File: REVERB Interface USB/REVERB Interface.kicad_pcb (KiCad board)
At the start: 2 copper layers, 90.2 x 95.9 mm, 74 parts, among them J1 RPiZeroW, J2 Iridium, J3 APRS, J4 Antenna, J6 USB_B_Micro, J7 USB, J8 USBPOGO, M1 MountingHole_Pad, M2 MountingHole_Pad, M3 MountingHole_Pad, M4 MountingHole_Pad, M5 PiMount, M6 PiMount, M7 PiMount, M8 PiMount, U1 IMU, U2 MAX3232, U3 CY7C65213-28PVXI, U4 TXB0104D, U5 DS3232M

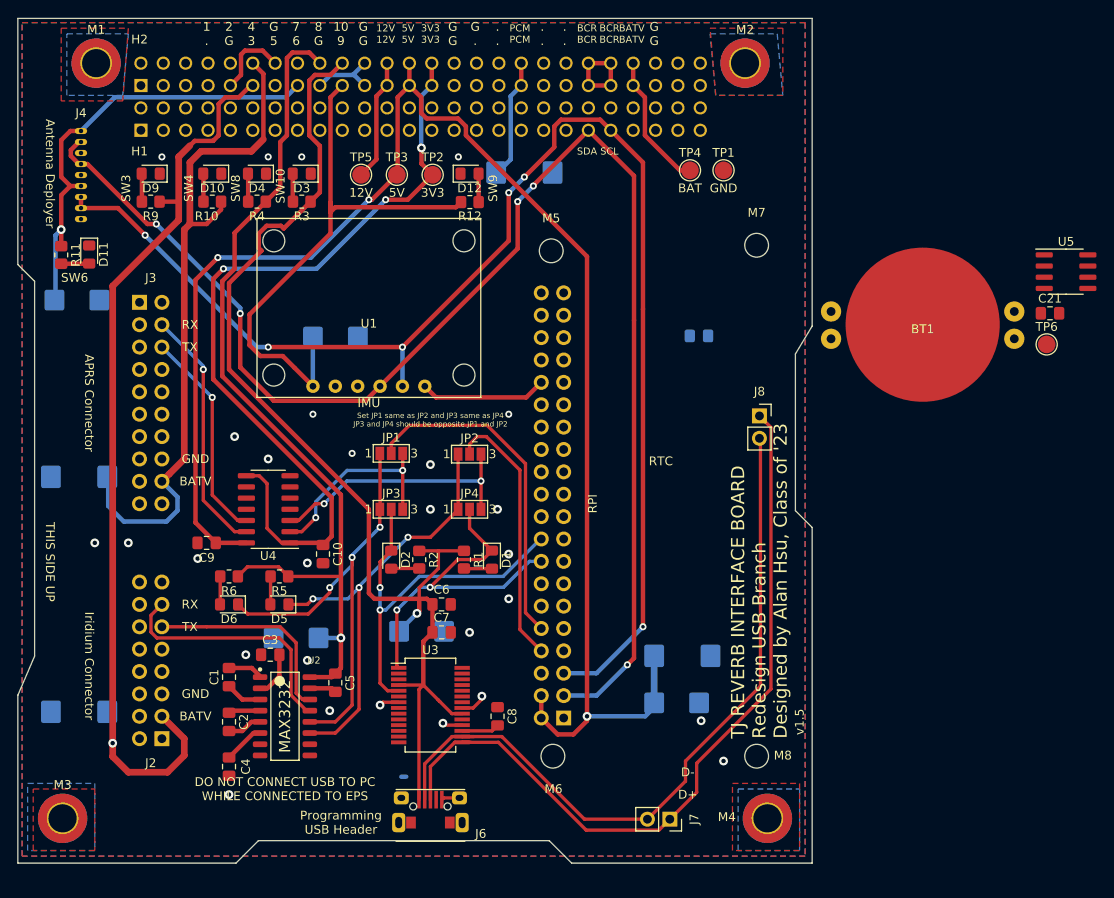
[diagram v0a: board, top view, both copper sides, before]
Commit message: add usb switch
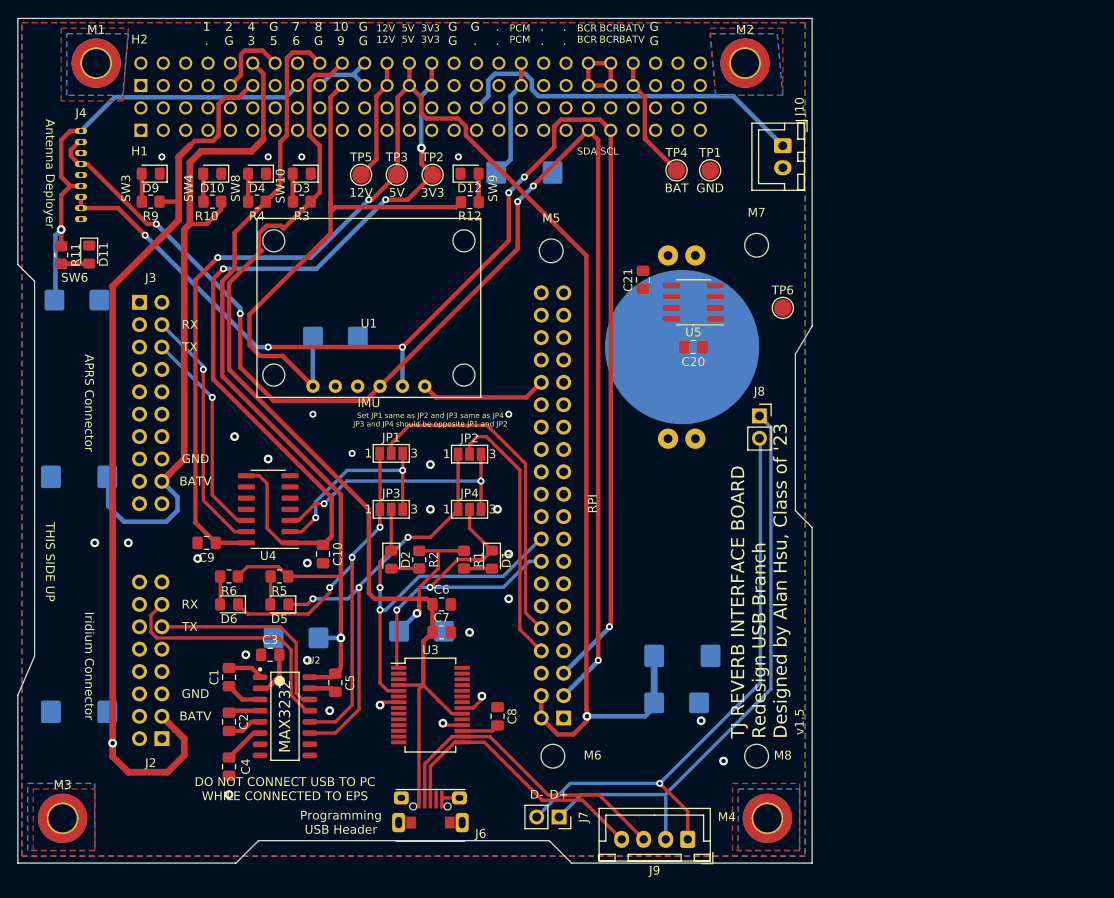
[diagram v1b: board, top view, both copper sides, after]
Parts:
- added J10: USBPWR, Connector_JST:JST_XH_B2B-XH-A_1x02_P2.50mm_Vertical, F.Cu at (193.7, 67.3)
- added J9: USB SWITCH, Connector_JST:JST_XH_B4B-XH-A_1x04_P2.50mm_Vertical, F.Cu at (182.9, 146.1)
- BT1: moved to B.Cu
- C20: moved to F.Cu
- moved C21 46.4 mm to (177.8, 82.5), turned to 90 degrees
- moved U5 42.5 mm to (183.5, 85.1), turned to 180 degrees
- moved TP6 30.2 mm to (193.7, 85.7)
- moved BT1 27.4 mm to (182.2, 90.2), turned to 90 degrees
- moved J7 12.6 mm to (168.3, 143.5)
- moved TP1 1.52 mm to (185.4, 70.1)
- moved TP4 1.52 mm to (181.6, 70.1)
- moved C20 1.42 mm to (183.5, 90.2)
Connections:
- H1 pad 32: (no net) -> /5VUSBCHG
- J7 pad 1: /D+ -> /PID+
- J7 pad 2: /D- -> /PID-
- J8 pad 1: /D+ -> /PID+
- J8 pad 2: /D- -> /PID-
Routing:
- net /PID-: track 0.00 -> 67.2 mm, vias 0 -> 1
- net /PID+: track 0.00 -> 66.6 mm
- net /D+: track 88.7 -> 32.1 mm
- net /D-: track 84.5 -> 36.4 mm
- net /5VUSBCHG: track 0.00 -> 41.4 mm
- net /EPSSDA: track 164.1 -> 158.6 mm
- net /EPSSCL: track 157.2 -> 152.0 mm
- net VBUS: track 15.5 -> 14.2 mm
- net /RI: track 0.57 -> 0.00 mm
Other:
- board text removed: "RTC"

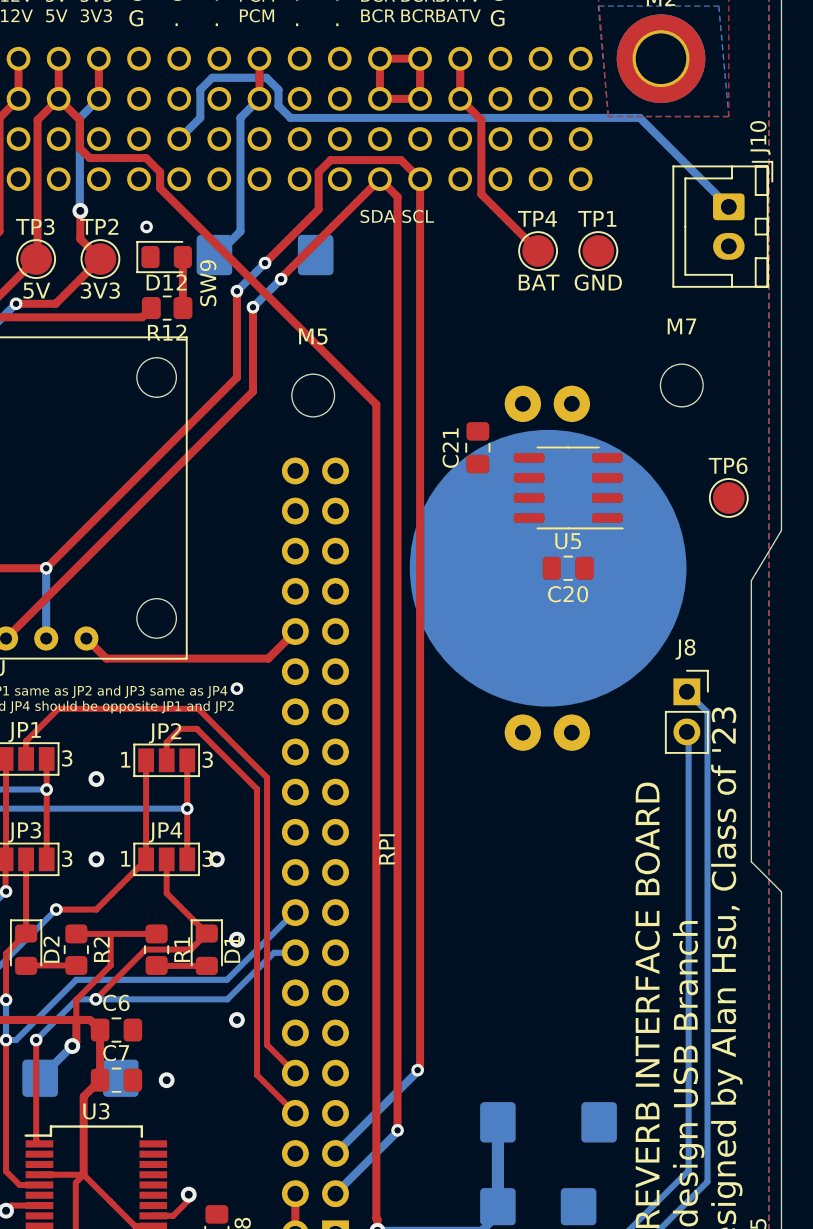
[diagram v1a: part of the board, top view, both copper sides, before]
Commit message: finish routing rtc
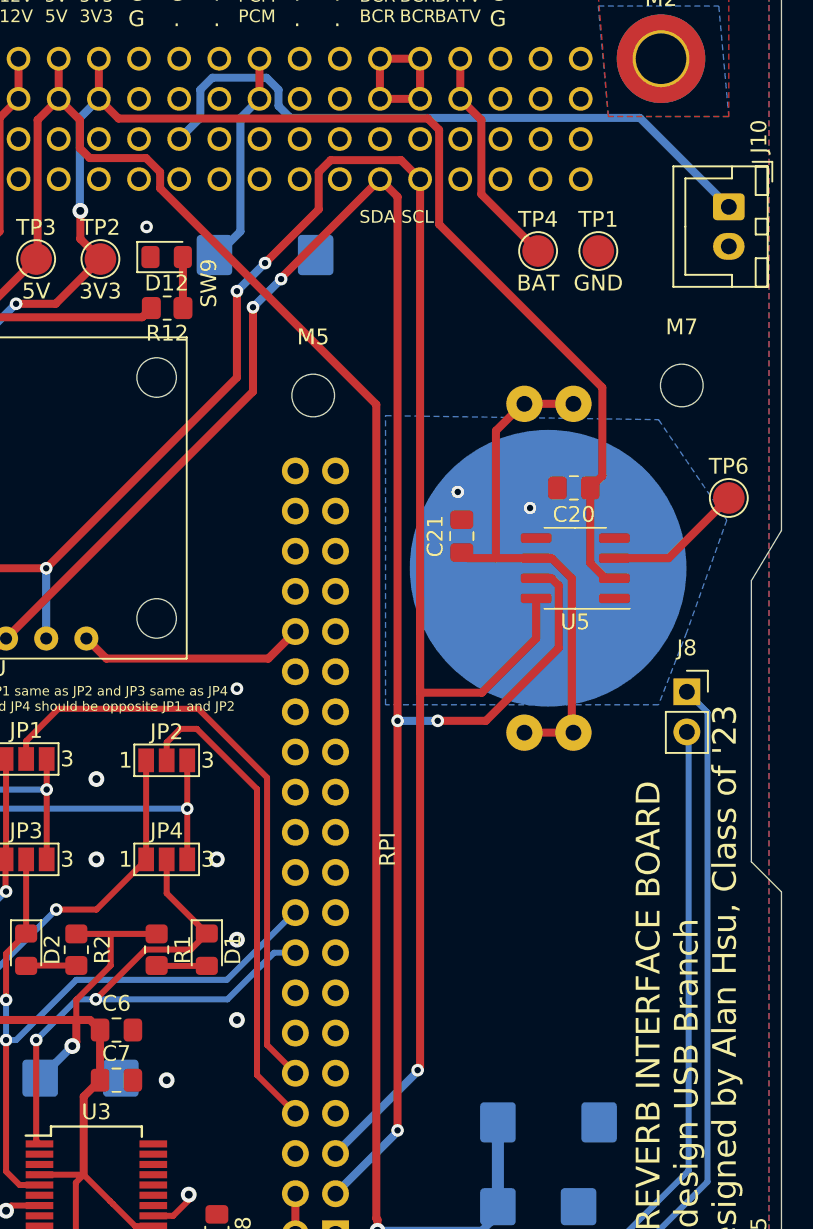
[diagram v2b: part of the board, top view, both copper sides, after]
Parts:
- moved C21 5.68 mm to (176.8, 88.1)
- moved U5 5.10 mm to (184.0, 90.2)
- moved C20 5.09 mm to (183.9, 85.1)
- turned BT1 to 270 degrees
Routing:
- net +3V3: track 94.6 -> 150.9 mm
- net Net-(BT1-Pad1): track 0.00 -> 34.2 mm
- net /EPSSDA: track 158.6 -> 176.2 mm, vias 5 -> 7
- net /EPSSCL: track 152.0 -> 169.3 mm
- net /SQW: track 0.00 -> 8.82 mm
- net GND: vias 28 -> 30

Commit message: Move some parts around, remove UART LEDs, .step export, push v1.6
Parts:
- removed D1, D5: RED, LED_SMD:LED_0805_2012Metric_Pad1.15x1.40mm_HandSolder
- removed D2, D6: GREEN, LED_SMD:LED_0805_2012Metric_Pad1.15x1.40mm_HandSolder
- removed R1, R2, R5, R6: 1K, Resistor_SMD:R_0805_2012Metric_Pad1.20x1.40mm_HandSolder
- moved R11 9.26 mm to (109.0, 70.9), turned to 180 degrees
- moved D11 8.14 mm to (109.1, 74.0), turned to 180 degrees
- moved C9 7.97 mm to (132.1, 119.4), turned to 0 degrees
- moved C13 4.86 mm to (176.8, 130.0)
- moved C11 4.83 mm to (177.5, 124.2)
- moved U4 4.20 mm to (133.5, 112.4)
- moved C10 3.92 mm to (140.2, 117.4)
- moved C16 3.85 mm to (112.0, 81.3), turned to 270 degrees
- moved JP1 3.21 mm to (146.2, 101.2)
- moved JP2 3.21 mm to (155.1, 101.3)
- moved JP3 3.21 mm to (146.2, 107.6)
- moved JP4 3.21 mm to (155.1, 107.6)
- moved J3 3.18 mm to (117.5, 85.1)
- moved J2 3.17 mm to (120.0, 134.6)
- moved BT1 2.29 mm to (180.0, 90.2)
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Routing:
- net /R1OUT: track 52.5 -> 35.9 mm, vias 3 -> 2
- net /SW8: track 101.5 -> 88.7 mm
- net /SW10: track 133.0 -> 120.4 mm
- net +5V: track 180.4 -> 188.8 mm
- net /T1IN: track 50.7 -> 42.7 mm, vias 3 -> 2
- net /APRSTXSh: track 24.2 -> 30.8 mm
- net /SW6: track 51.7 -> 45.2 mm
- net /APRSRXSh: track 28.2 -> 34.6 mm
- net /USBUARTTX: track 39.8 -> 34.0 mm
- net +3V3: track 150.9 -> 155.9 mm
- net /SW3: track 108.9 -> 105.1 mm
- net /APRSRX: track 23.1 -> 26.9 mm
- net /R1IN: track 28.3 -> 31.6 mm
- net Net-(D2-Pad2): track 3.19 -> 0.00 mm
- net Net-(D1-Pad2): track 3.19 -> 0.00 mm
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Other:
- board text added: "G"
- board text added: "PI D+"
- board text added: "PI D-"
- board text added: "UARTD+"
- board text added: "UARTD-"
- board text added: "v1.6"
- board text removed: "v1.5"

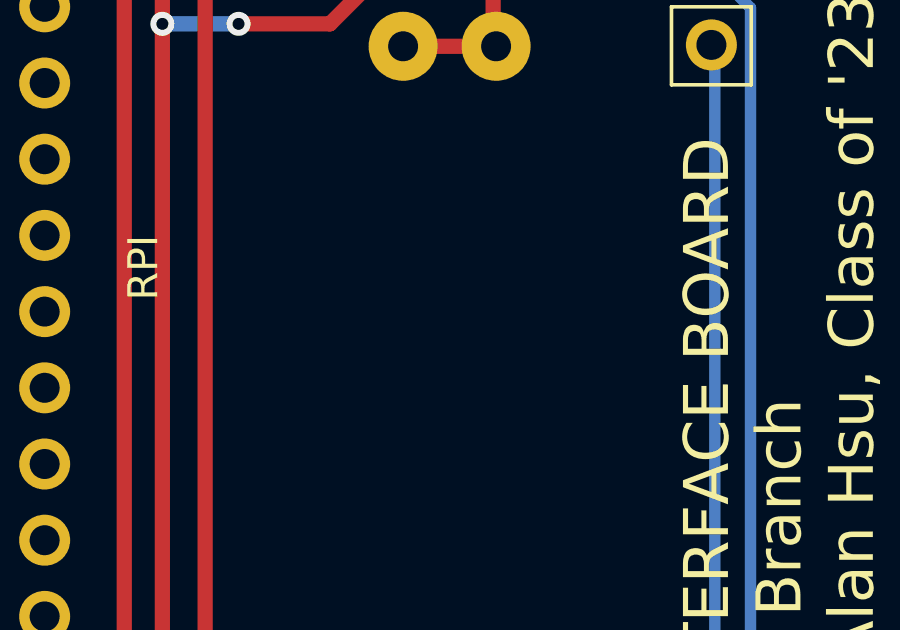
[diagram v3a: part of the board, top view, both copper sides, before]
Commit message: start on adding i2c-0 option
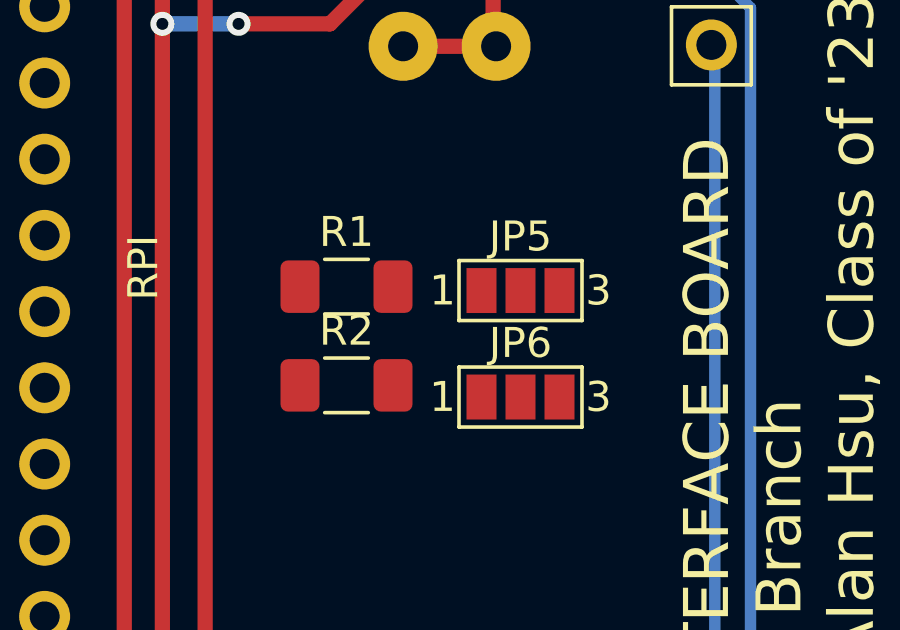
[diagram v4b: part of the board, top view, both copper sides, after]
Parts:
- added JP5: RTCSDA, Jumper:SolderJumper-3_P1.3mm_Open_Pad1.0x1.5mm_NumberLabels, F.Cu at (182.4, 108.7)
- added JP6: RTCSCL, Jumper:SolderJumper-3_P1.3mm_Open_Pad1.0x1.5mm_NumberLabels, F.Cu at (182.4, 112.3)
- added R1: 2.2K, Resistor_SMD:R_1206_3216Metric_Pad1.30x1.75mm_HandSolder, F.Cu at (176.6, 108.6)
- added R2: 2.2K, Resistor_SMD:R_1206_3216Metric_Pad1.30x1.75mm_HandSolder, F.Cu at (176.6, 111.9)
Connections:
- J1 pad 1: (no net) -> +3.3VA
- J1 pad 17: (no net) -> +3.3VA
- J1 pad 27: (no net) -> /SDA0
- J1 pad 28: (no net) -> /SCL0
- U5 pad 7: /EPSSDA -> /RTCSDA
- U5 pad 8: /EPSSCL -> /RTCSCL

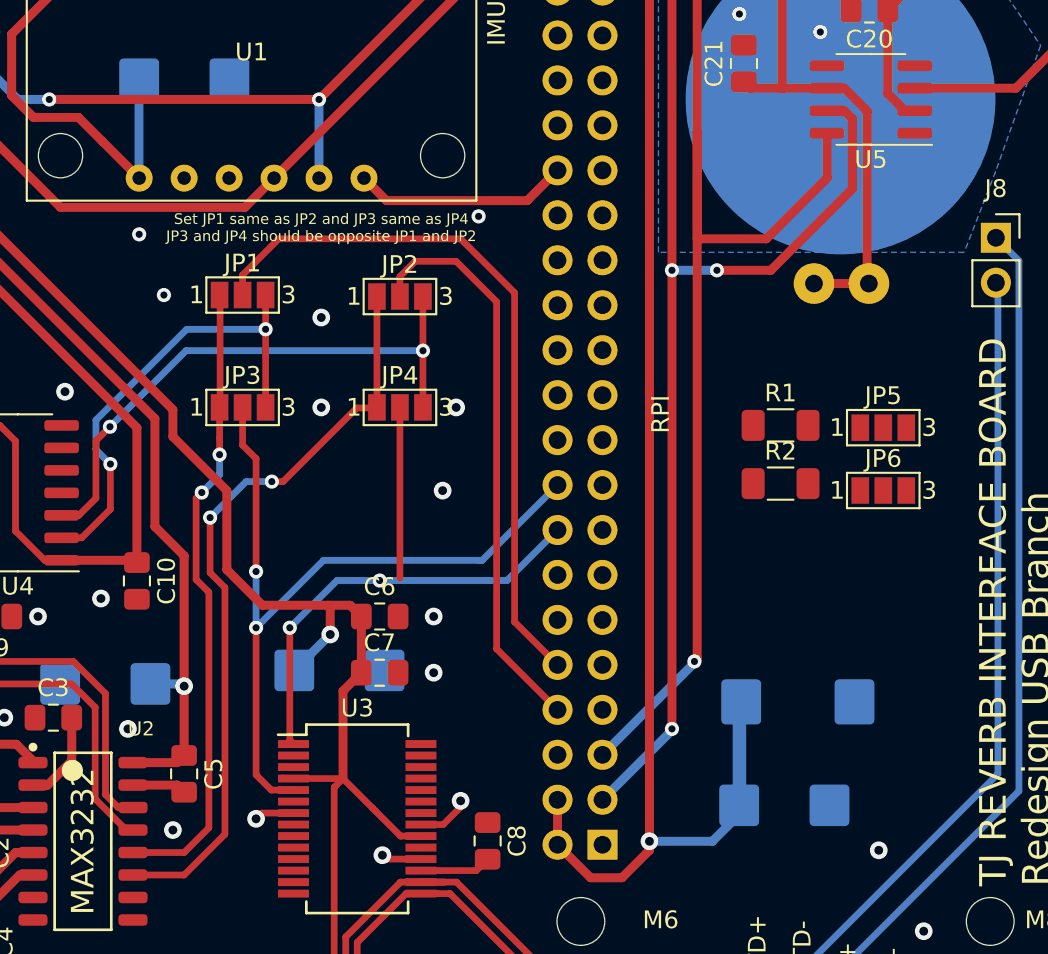
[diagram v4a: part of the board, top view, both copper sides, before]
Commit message: add i2c0 option
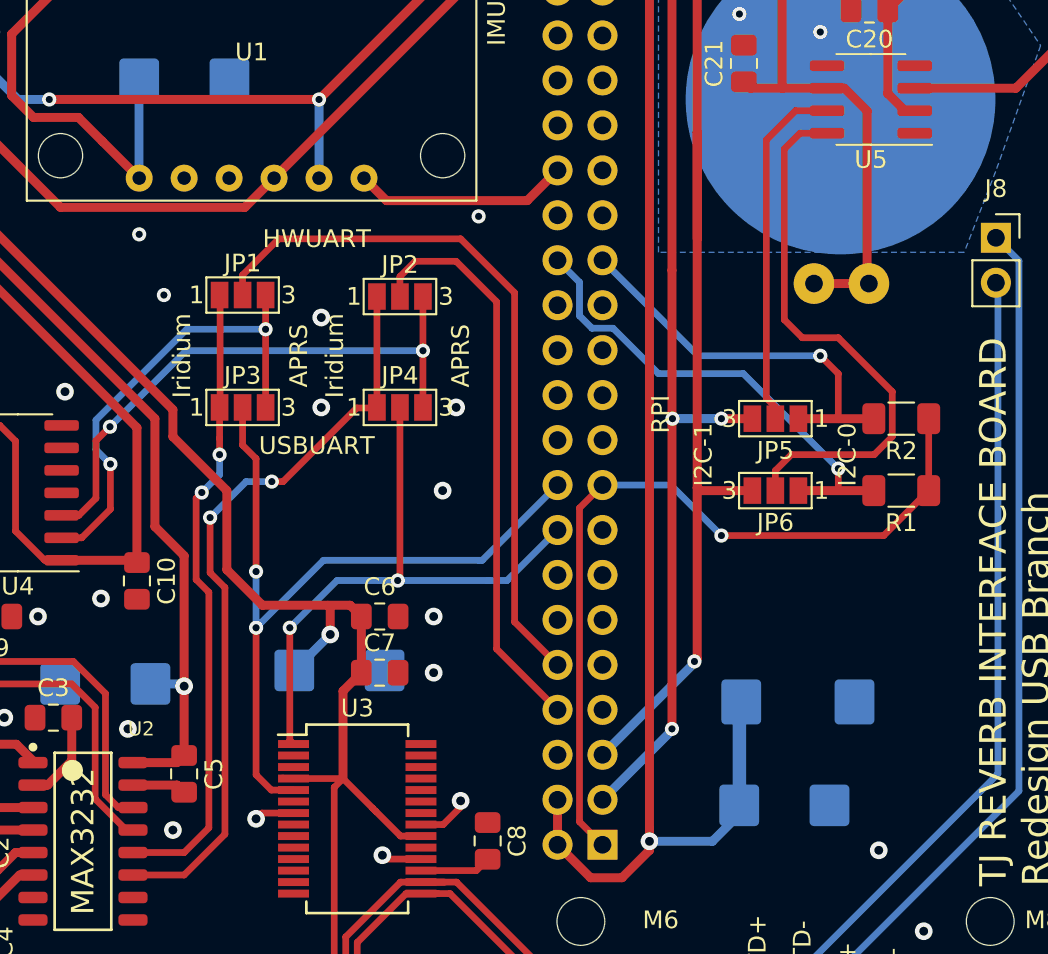
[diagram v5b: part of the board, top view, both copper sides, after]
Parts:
- moved R1 7.75 mm to (183.4, 112.3), turned to 180 degrees
- moved R2 7.74 mm to (183.4, 108.2), turned to 180 degrees
- moved JP5 6.12 mm to (176.3, 108.2), turned to 180 degrees
- moved JP6 6.10 mm to (176.3, 112.3), turned to 180 degrees
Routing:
- net +3.3VA: track 0.00 -> 46.1 mm, vias 0 -> 1
- net /RTCSCL: track 0.00 -> 31.3 mm
- net /SCL0: track 0.00 -> 27.4 mm, vias 0 -> 1
- net /SDA0: track 0.00 -> 22.8 mm, vias 0 -> 1
- net /RTCSDA: track 0.00 -> 20.1 mm
- net /EPSSDA: track 173.5 -> 160.3 mm
- net /EPSSCL: track 170.2 -> 162.1 mm
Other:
- board text added: "APRS"
- board text added: "HWUART"
- board text added: "I2C-0"
- board text added: "I2C-1"
- board text added: "Iridium"
- board text added: "USBUART"
- board text removed: "Set JP1 same as JP2 and JP3 same as JP4 JP3 and JP4 should be opposite JP1 and JP2"

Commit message: tidy up the schematic, for usb branch
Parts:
- M1, M2, M3, M4: value MountingHole_Pad -> Stack Mounting Hole
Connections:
- net /APRSRXSh renamed /APRSRX_Shift
- net /APRSTXSh renamed /APRSTX_Shift
- net Net-(BT1-Pad1) renamed +BATT

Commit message: new gerber exports
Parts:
- C13, C16: value 47uF -> 22uF
